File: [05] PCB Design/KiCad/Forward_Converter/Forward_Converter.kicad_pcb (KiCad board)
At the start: 2 copper layers, 75 parts, among them J1 Conn_01x02_Pin, J2 Conn_01x02_Pin, J3 Conn_01x02_Pin, J4 Conn_01x02_Pin, J5 Conn_01x02_Pin, Q1 CSD19534Q5A, Q2 CSD19534Q5A, Q3 BSC320N20NS3G, Q4 BCX56, Q5 BC857, Q6 BCX56, T1 P0926NL, T2 EE30157-Custom, U1 LT1952EGN-1-PBF, U2 LTC3900ES8-PBF, U3 MC7812CDTRKG, U4 LT4430ES6-TRPBF, U5 TCMT1106

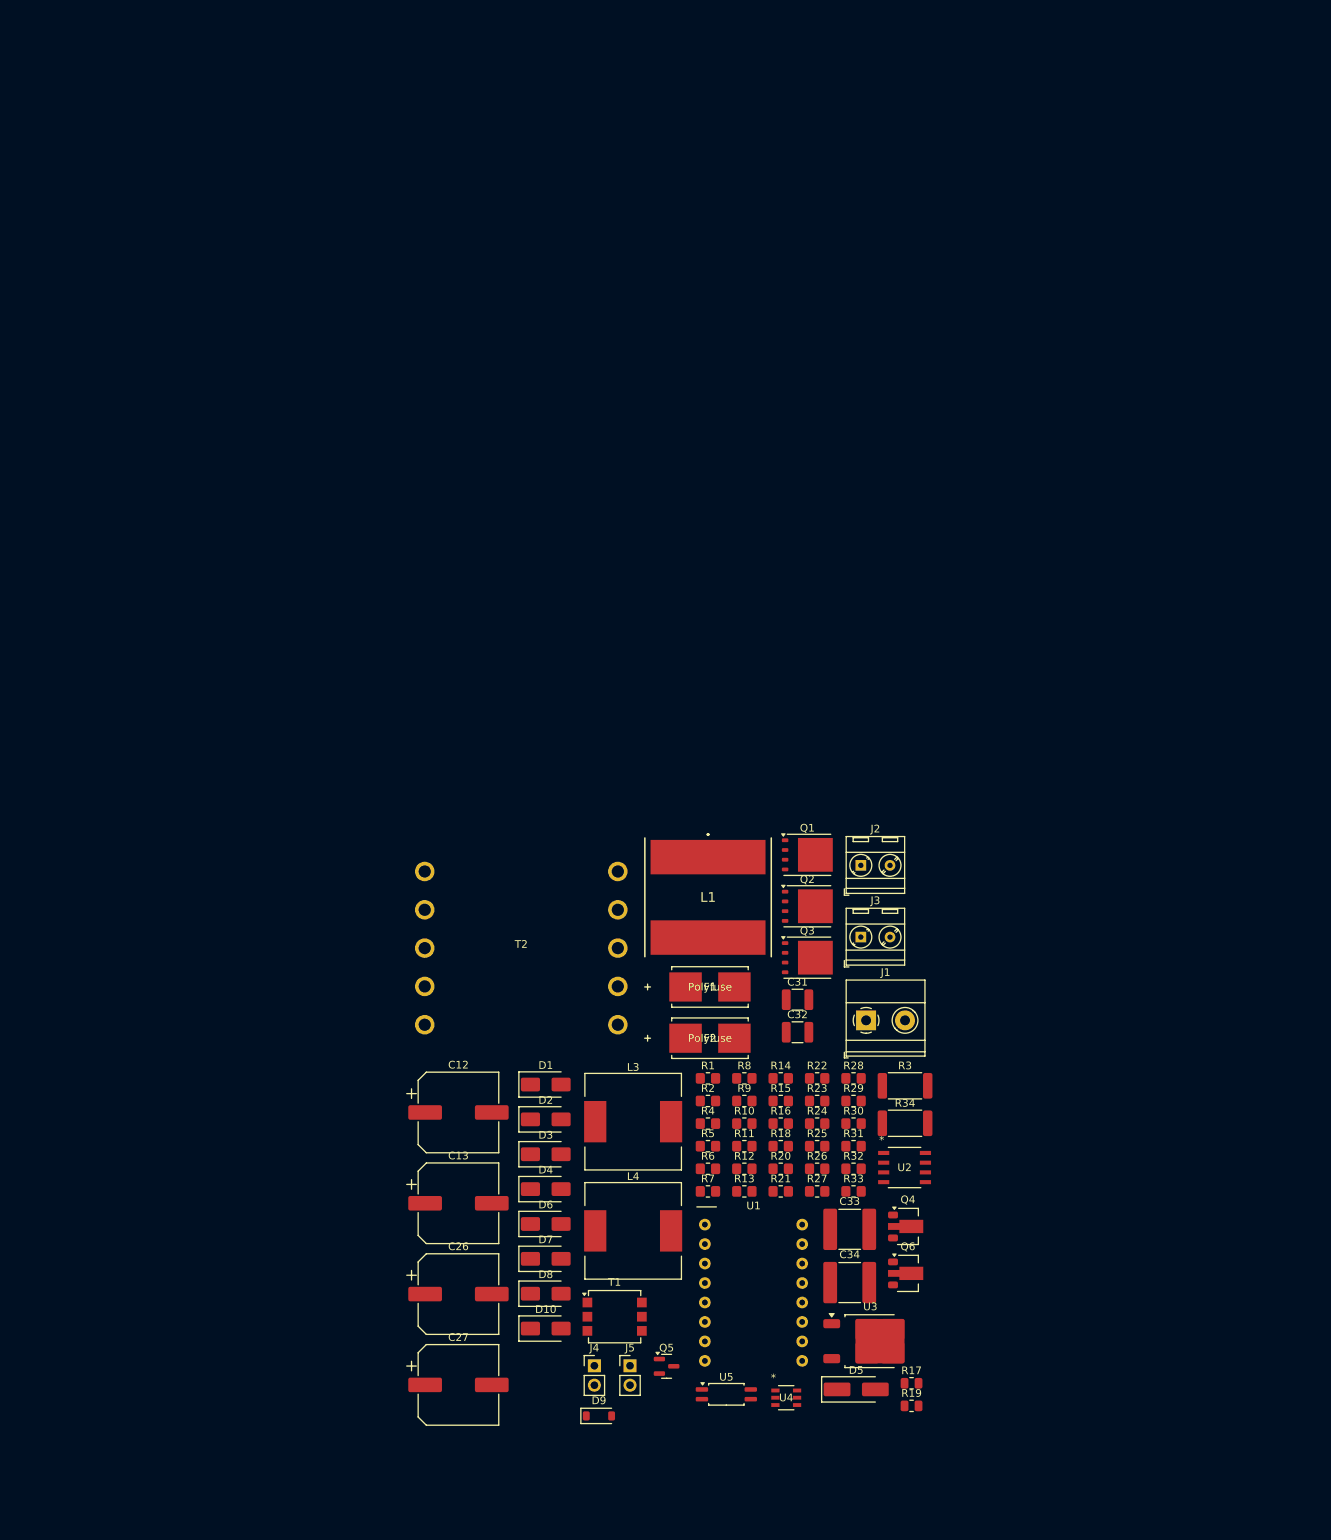
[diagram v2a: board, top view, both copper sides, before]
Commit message: Layout placement
Placement is almost complete connections to be completed.
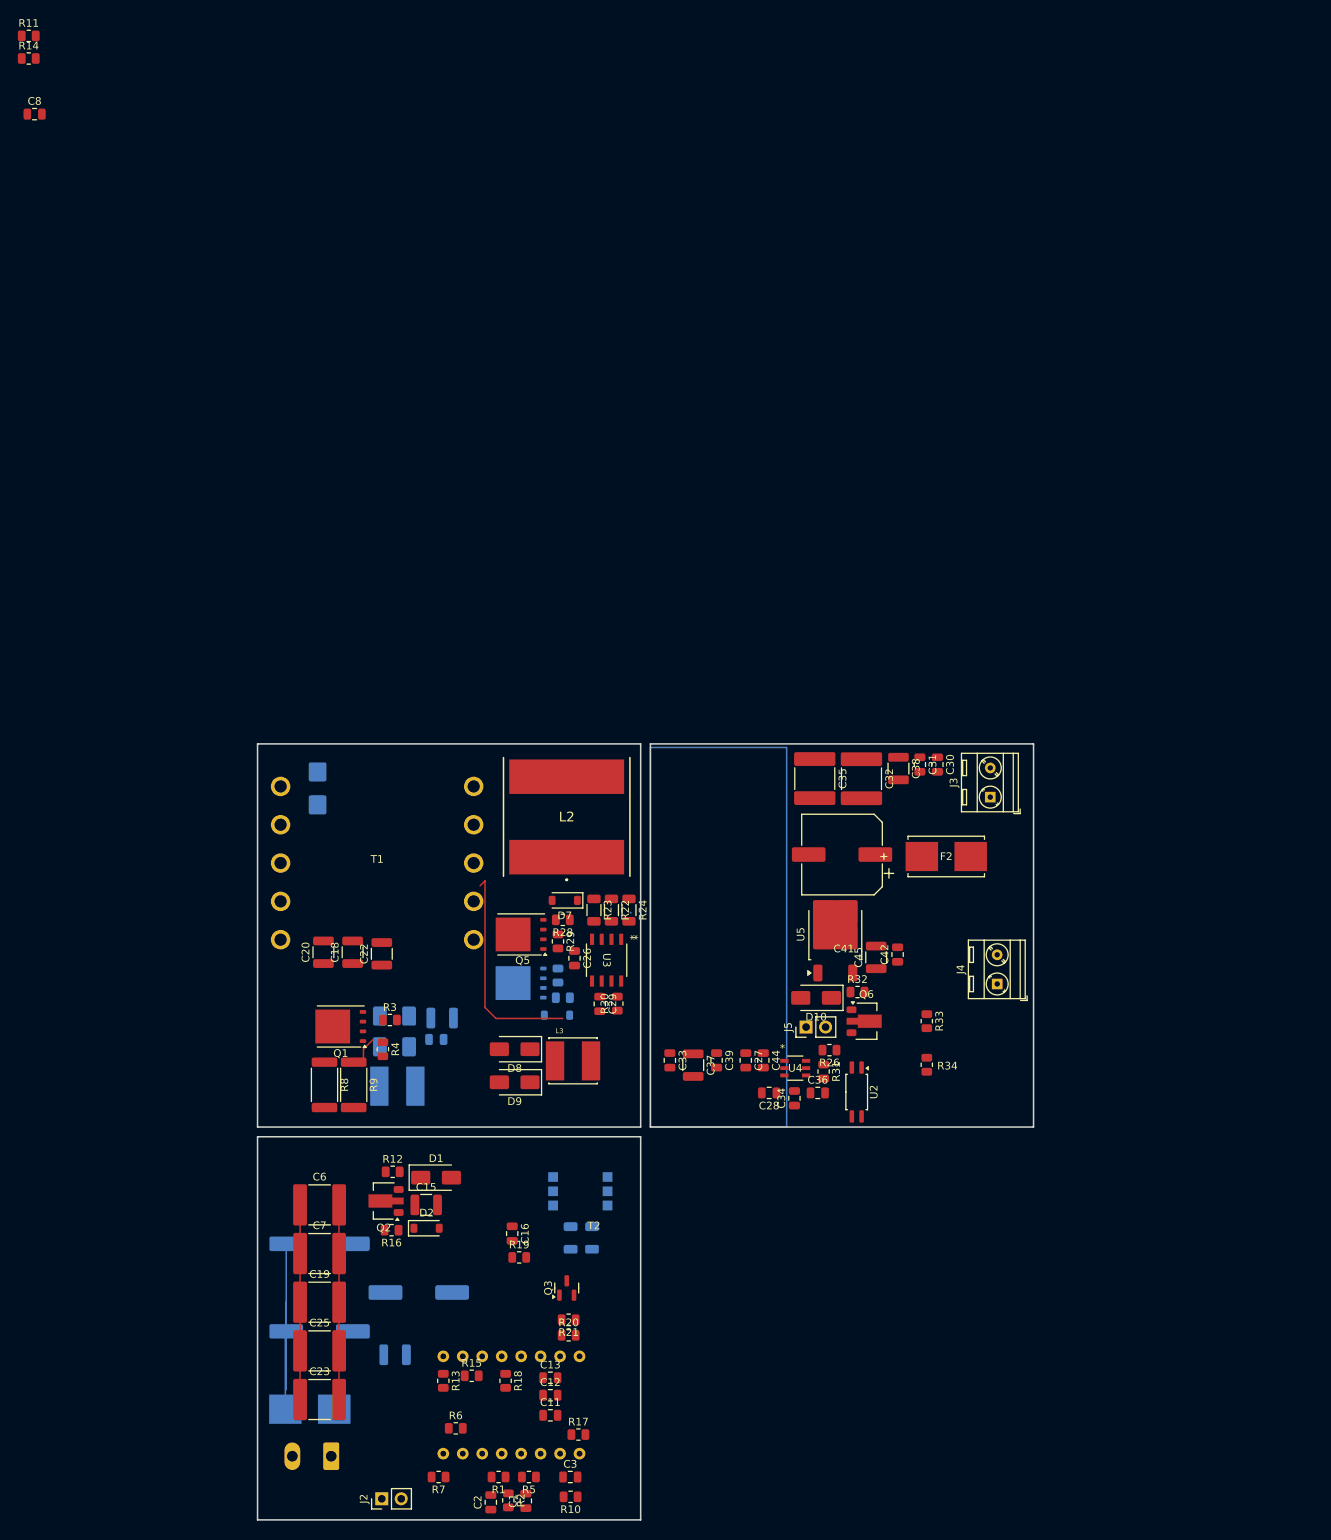
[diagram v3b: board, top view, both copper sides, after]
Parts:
- removed L4: 22uH, Inductor_SMD:L_12x12mm_H6mm
- added C1: 2.2nF, Capacitor_SMD:C_0805_2012Metric, F.Cu at (72.6, 125.0)
- added C10: 10u, Capacitor_SMD:C_1210_3225Metric, B.Cu at (55.6, 105.9)
- added C11: 2.2uF, Capacitor_SMD:C_0805_2012Metric, F.Cu at (75.8, 113.8)
- added C14: 10u, Capacitor_SMD:C_1210_3225Metric, B.Cu at (61.7, 62.0)
- added C15: 1uF, Capacitor_SMD:C_1210_3225Metric, F.Cu at (59.6, 86.4)
- added C16: 2.2nF, Capacitor_SMD:C_0805_2012Metric, F.Cu at (70.9, 90.1)
- added C17: 100n, Capacitor_SMD:C_0805_2012Metric, B.Cu at (61.0, 64.8)
- added C18: 1uF, Capacitor_SMD:C_1210_3225Metric, F.Cu at (50.0, 53.4)
- added C19: 2.2u, Capacitor_SMD:C_2220_5750Metric, F.Cu at (45.7, 99.1)
- added C2: 100nF, Capacitor_SMD:C_0805_2012Metric, F.Cu at (68.1, 125.2)
- added C20: 1uF, Capacitor_SMD:C_1210_3225Metric, F.Cu at (46.2, 53.4)
- added C21: 100pF, Capacitor_SMD:C_1206_3216Metric, B.Cu at (81.3, 90.7)
- added C22: 1uF, Capacitor_SMD:C_1210_3225Metric, F.Cu at (53.8, 53.6)
- added C23: 2.2u, Capacitor_SMD:C_2220_5750Metric, F.Cu at (45.7, 111.8)
- added C24: 220pF, Capacitor_SMD:C_1206_3216Metric, B.Cu at (78.5, 90.7)
- added C25: 2.2u, Capacitor_SMD:C_2220_5750Metric, F.Cu at (45.7, 105.4)
- added C28: 100p, Capacitor_SMD:C_0805_2012Metric, F.Cu at (104.4, 71.8)
- added C29: 470p, Capacitor_SMD:C_0805_2012Metric, F.Cu at (82.3, 60.1)
- added C3: OC, Capacitor_SMD:C_0805_2012Metric, F.Cu at (78.4, 121.9)
- added C30: 100n, Capacitor_SMD:C_0805_2012Metric, F.Cu at (126.4, 28.9)
- added C35: 2.2u, Capacitor_SMD:C_2220_5750Metric, F.Cu at (110.4, 30.7)
- added C36: 10n, Capacitor_SMD:C_0805_2012Metric, F.Cu at (110.7, 71.8)
- added C37: 10u, Capacitor_SMD:C_1210_3225Metric, F.Cu at (94.5, 68.1)
- added C38: 22u, Capacitor_SMD:C_1210_3225Metric, F.Cu at (121.3, 29.4)
- added C39: 100n, Capacitor_SMD:C_0805_2012Metric, F.Cu at (97.5, 67.5)
- added C4: 47u, Capacitor_SMD:CP_Elec_10x12.6, B.Cu at (45.7, 91.4)
- added C41: 180u, Capacitor_SMD:CP_Elec_10x12.6, F.Cu at (113.9, 40.6)
- added C42: 100n, Capacitor_SMD:C_0805_2012Metric, F.Cu at (121.2, 53.7)
- added C44: 100n, Capacitor_SMD:C_0805_2012Metric, F.Cu at (103.6, 67.5)
- added C45: 10u, Capacitor_SMD:C_1210_3225Metric, F.Cu at (118.4, 54.1)
- added C5: 47u, Capacitor_SMD:CP_Elec_10x12.6, B.Cu at (45.7, 102.9)
- added C6: 2.2uF, Capacitor_SMD:C_2220_5750Metric, F.Cu at (45.7, 86.4)
- added C7: 2.2uF, Capacitor_SMD:C_2220_5750Metric, F.Cu at (45.7, 92.7)
- added C8: 2.2nF, Capacitor_SMD:C_0805_2012Metric, F.Cu at (8.54, -56.0)
- added C9: 47u, Capacitor_SMD:CP_Elec_10x12.6, B.Cu at (58.7, 97.8)
- added L2: 22uH, Forward_Footprint:SRP1513CA8R2M_V2, F.Cu at (78.0, 35.7)
- C12, C13: value 180u -> 100nF; footprint Capacitor_SMD:CP_Elec_10x12.6 -> Capacitor_SMD:C_0805_2012Metric
- C26: value 47u -> 100n; footprint Capacitor_SMD:CP_Elec_10x12.6 -> Capacitor_SMD:C_0805_2012Metric
- C27: value 47u -> 1uF; footprint Capacitor_SMD:CP_Elec_10x12.6 -> Capacitor_SMD:C_0805_2012Metric
- C31: value 1uF -> 100n; footprint Capacitor_SMD:C_1210_3225Metric -> Capacitor_SMD:C_0805_2012Metric
- C32: value 1uF -> 2.2u; footprint Capacitor_SMD:C_1210_3225Metric -> Capacitor_SMD:C_2220_5750Metric
- C33: value 2.2u -> 100n; footprint Capacitor_SMD:C_2220_5750Metric -> Capacitor_SMD:C_0805_2012Metric
- C34: value 2.2u -> 220p; footprint Capacitor_SMD:C_2220_5750Metric -> Capacitor_SMD:C_0805_2012Metric
- D1: value MS110 -> 1SMA5931
- D10: value 1SMA5931 -> SMAJ4737A
- D2: value MS110 -> BZT52C12-TP; footprint Diode_SMD:D_SMA -> Diode_SMD:D_SOD-123
- D3, F1, U1: moved to B.Cu
- D4: value MS110 -> BR320; footprint Diode_SMD:D_SMA -> Diode_SMD:D_SMB; moved to B.Cu
- D5: value SMAJ4737A -> MS110; footprint Diode_SMD:D_SMA_Handsoldering -> Diode_SMD:D_SMA; moved to B.Cu
- D6: footprint Diode_SMD:D_SMA -> Diode_SMD:D_SOD-123; moved to B.Cu
- D7: footprint Diode_SMD:D_SMA -> Diode_SMD:D_SOD-123
- D8: value BR320 -> MS110
- D9: value BZT52C12-TP -> MS110; footprint Diode_SMD:D_SOD-123 -> Diode_SMD:D_SMA
- J1: value Conn_01x02_Pin -> INPUT; footprint TerminalBlock_Phoenix:TerminalBlock_Phoenix_MKDS-1,5-2-5.08_1x02_P5.08mm_Horizontal -> Connector_Phoenix_MSTB:PhoenixContact_MSTBA_2,5_2-G-5,08_1x02_P5.08mm_Horizontal; moved to B.Cu
- J2: value Conn_01x02_Pin -> BIAS; footprint TerminalBlock_MetzConnect:TerminalBlock_MetzConnect_Type086_RT03402HBLC_1x02_P3.81mm_Horizontal -> Connector_PinHeader_2.54mm:PinHeader_1x02_P2.54mm_Vertical
- J3: value Conn_01x02_Pin -> OUTPUT
- J4: value Conn_01x02_Pin -> AUX; footprint Connector_PinHeader_2.54mm:PinHeader_1x02_P2.54mm_Vertical -> TerminalBlock_MetzConnect:TerminalBlock_MetzConnect_Type086_RT03402HBLC_1x02_P3.81mm_Horizontal
- J5: value Conn_01x02_Pin -> 8V
- L1: value 22uH -> 10uH; footprint Forward_Footprint:SRP1513CA8R2M_V2 -> Forward_Footprint:IND_VLS6045EX-100M-H; moved to B.Cu
- L3: value 22uH -> 10uH; footprint Inductor_SMD:L_12x12mm_H6mm -> Forward_Footprint:IND_VLS6045EX-100M-H
- Q1: value CSD19534Q5A -> BSC320N20NS3G
- Q2: value CSD19534Q5A -> BCX56; footprint Package_TO_SOT_SMD:TDSON-8-1 -> Package_TO_SOT_SMD:SOT-89-3
- Q3: value BSC320N20NS3G -> BC857; footprint Package_TO_SOT_SMD:TDSON-8-1 -> Package_TO_SOT_SMD:SOT-23
- Q4: value BCX56 -> CSD19534Q5A; footprint Package_TO_SOT_SMD:SOT-89-3 -> Package_TO_SOT_SMD:TDSON-8-1; moved to B.Cu
- Q5: value BC857 -> CSD19534Q5A; footprint Package_TO_SOT_SMD:SOT-23 -> Package_TO_SOT_SMD:TDSON-8-1
- R1: value 12R -> 12k; footprint Resistor_SMD:R_0805_2012Metric_Pad1.20x1.40mm_HandSolder -> Resistor_SMD:R_0805_2012Metric
- R10: value 180k -> 10k; footprint Resistor_SMD:R_0805_2012Metric_Pad1.20x1.40mm_HandSolder -> Resistor_SMD:R_0805_2012Metric
- R11: value 100k -> 0; footprint Resistor_SMD:R_0805_2012Metric_Pad1.20x1.40mm_HandSolder -> Resistor_SMD:R_0805_2012Metric
- R12: value 160k -> 4.7k; footprint Resistor_SMD:R_0805_2012Metric_Pad1.20x1.40mm_HandSolder -> Resistor_SMD:R_0805_2012Metric
- R13: value 10k -> 100k; footprint Resistor_SMD:R_0805_2012Metric_Pad1.20x1.40mm_HandSolder -> Resistor_SMD:R_0805_2012Metric
- R14: value 10k -> 0; footprint Resistor_SMD:R_0805_2012Metric_Pad1.20x1.40mm_HandSolder -> Resistor_SMD:R_0805_2012Metric
- R15: value 10k -> 0R; footprint Resistor_SMD:R_0805_2012Metric_Pad1.20x1.40mm_HandSolder -> Resistor_SMD:R_0805_2012Metric
- R16: value 25 -> 4.7k; footprint Resistor_SMD:R_0805_2012Metric_Pad1.20x1.40mm_HandSolder -> Resistor_SMD:R_0805_2012Metric
- R17: value 22k -> 10k
- R18: value 25 -> 160k; footprint Resistor_SMD:R_0805_2012Metric_Pad1.20x1.40mm_HandSolder -> Resistor_SMD:R_0805_2012Metric
- R19: value 22k -> 47R
- R2: value 10k -> 18k; footprint Resistor_SMD:R_0805_2012Metric_Pad1.20x1.40mm_HandSolder -> Resistor_SMD:R_0805_2012Metric
- R20: value 47R -> 220R; footprint Resistor_SMD:R_0805_2012Metric_Pad1.20x1.40mm_HandSolder -> Resistor_SMD:R_0805_2012Metric
- R21: value 200k -> 1.2k; footprint Resistor_SMD:R_0805_2012Metric_Pad1.20x1.40mm_HandSolder -> Resistor_SMD:R_0805_2012Metric
- R22: value 27k -> 360; footprint Resistor_SMD:R_0805_2012Metric_Pad1.20x1.40mm_HandSolder -> Resistor_SMD:R_1206_3216Metric
- R23: value 8.2k -> 182; footprint Resistor_SMD:R_0805_2012Metric_Pad1.20x1.40mm_HandSolder -> Resistor_SMD:R_1206_3216Metric
- R24: value 4.7k -> 365; footprint Resistor_SMD:R_0805_2012Metric_Pad1.20x1.40mm_HandSolder -> Resistor_SMD:R_1206_3216Metric
- R25: value 1.2k -> 25; footprint Resistor_SMD:R_0805_2012Metric_Pad1.20x1.40mm_HandSolder -> Resistor_SMD:R_0805_2012Metric; moved to B.Cu
- R26: value 220R -> 4.7k; footprint Resistor_SMD:R_0805_2012Metric_Pad1.20x1.40mm_HandSolder -> Resistor_SMD:R_0805_2012Metric
- R27: value 10k -> 22k; footprint Resistor_SMD:R_0805_2012Metric_Pad1.20x1.40mm_HandSolder -> Resistor_SMD:R_0805_2012Metric; moved to B.Cu
- R28: value 1k -> 25; footprint Resistor_SMD:R_0805_2012Metric_Pad1.20x1.40mm_HandSolder -> Resistor_SMD:R_0805_2012Metric
- R29: value 4.7k -> 22k; footprint Resistor_SMD:R_0805_2012Metric_Pad1.20x1.40mm_HandSolder -> Resistor_SMD:R_0805_2012Metric
- R3: value 15m -> 12R; footprint Resistor_SMD:R_2512_6332Metric -> Resistor_SMD:R_0805_2012Metric
- R30: value 4.7k -> 100k; footprint Resistor_SMD:R_0805_2012Metric_Pad1.20x1.40mm_HandSolder -> Resistor_SMD:R_0805_2012Metric
- R31: value 0R -> 8.2k; footprint Resistor_SMD:R_0805_2012Metric_Pad1.20x1.40mm_HandSolder -> Resistor_SMD:R_0805_2012Metric
- R32: value 0 -> 1k; footprint Resistor_SMD:R_0805_2012Metric_Pad1.20x1.40mm_HandSolder -> Resistor_SMD:R_0805_2012Metric
- R33: value 0 -> 200k; footprint Resistor_SMD:R_0805_2012Metric_Pad1.20x1.40mm_HandSolder -> Resistor_SMD:R_0805_2012Metric
- R34: value 15m -> 27k; footprint Resistor_SMD:R_2512_6332Metric -> Resistor_SMD:R_0805_2012Metric
- R4: value 12k -> 10k; footprint Resistor_SMD:R_0805_2012Metric_Pad1.20x1.40mm_HandSolder -> Resistor_SMD:R_0805_2012Metric
- R5: value 10k -> 180k; footprint Resistor_SMD:R_0805_2012Metric_Pad1.20x1.40mm_HandSolder -> Resistor_SMD:R_0805_2012Metric
- R6: footprint Resistor_SMD:R_0805_2012Metric_Pad1.20x1.40mm_HandSolder -> Resistor_SMD:R_0805_2012Metric
- R7: value 18k -> 10k; footprint Resistor_SMD:R_0805_2012Metric_Pad1.20x1.40mm_HandSolder -> Resistor_SMD:R_0805_2012Metric
- R8: value 47R -> 15m; footprint Resistor_SMD:R_0805_2012Metric_Pad1.20x1.40mm_HandSolder -> Resistor_SMD:R_2512_6332Metric
- R9: value 10k -> 15m; footprint Resistor_SMD:R_0805_2012Metric_Pad1.20x1.40mm_HandSolder -> Resistor_SMD:R_2512_6332Metric
- T1: value P0926NL -> EE30157-Custom; footprint Transformer_SMD:Pulse_P0926NL -> Forward_Footprint:EE30157-Custom
- T2: value EE30157-Custom -> P0926NL; footprint Forward_Footprint:EE30157-Custom -> Transformer_SMD:Pulse_P0926NL; moved to B.Cu
- U2: value LTC3900ES8-PBF -> TCMT1106; footprint Forward_Footprint:SO-8_S_LIT -> Package_SO:SOP-4_4.4x2.6mm_P1.27mm
- U3: value MC7812CDTRKG -> LTC3900ES8-PBF; footprint Package_TO_SOT_SMD:TO-252-2 -> Forward_Footprint:SO-8_S_LIT
- U5: value TCMT1106 -> MC7812CDTRKG; footprint Package_SO:SOP-4_4.4x2.6mm_P1.27mm -> Package_TO_SOT_SMD:TO-252-2
- moved R11 172.4 mm to (7.77, -66.2)
- moved R14 165.4 mm to (7.77, -63.2)
- moved J2 103.6 mm to (53.8, 124.7), turned to 90 degrees
- moved J1 90.0 mm to (47.2, 119.2), turned to 180 degrees
- moved D5 77.8 mm to (53.6, 63.7), turned to 90 degrees
- moved F1 75.9 mm to (44.5, 113.0), turned to 180 degrees
- moved J4 72.4 mm to (134.2, 57.5), turned to 90 degrees
- moved R3 67.8 mm to (54.9, 62.2)
- moved Q2 67.3 mm to (54.1, 85.9), turned to 180 degrees
- moved T1 66.8 mm to (53.2, 41.8)
- moved Q1 64.9 mm to (48.5, 63.1), turned to 180 degrees
- moved U5 61.7 mm to (113.0, 51.1), turned to 90 degrees
- moved U3 60.5 mm to (83.2, 54.4), turned to -90 degrees
- moved D4 60.2 mm to (45.5, 32.0), turned to 90 degrees
- moved Q4 59.6 mm to (72.0, 57.4), turned to 180 degrees
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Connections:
- C12 pad 1: /5V -> GND
- C12 pad 2: GNDPWR -> /Vbias
- C13 pad 1: /5V -> GND
- C13 pad 2: GNDPWR -> /Vbias
- C26 pad 1: Vin -> /8V
- C26 pad 2: PGND -> GNDSEC
- C27 pad 1: Vin -> /8V
- C27 pad 2: PGND -> GNDSEC
- C31 pad 1: Vin -> /5V
- C31 pad 2: PGND -> GNDPWR
- C32 pad 1: Vin -> /5V
- C32 pad 2: PGND -> GNDPWR
- C33 pad 1: Vin -> Net-(U5-VI)
- C33 pad 2: PGND -> GNDSEC
- C34 pad 1: Vin -> Net-(U4-FB)
- C34 pad 2: PGND -> Net-(U4-COMP)
- D1 pad 1: Net-(D1-K) -> /Vbias
- D10 pad 1: /Vbias -> Net-(D10-A1)
- D10 pad 2: GND -> GNDSEC
- D2 pad 2: GNDSEC -> GND
- D3 pad 1: Net-(D2-K) -> Net-(D3-K)
- D3 pad 2: /Vaux -> GND
- D4 pad 1: Net-(D1-K) -> /RST
- D4 pad 2: /AUX -> PGND
- D5 pad 1: Net-(D5-A1) -> Net-(D3-K)
- D5 pad 2: GNDSEC -> /AUX
- D8 pad 1: /RST -> Net-(D8-K)
- D8 pad 2: PGND -> /Vaux
- D9 pad 1: Net-(D9-K) -> Net-(D8-K)
- D9 pad 2: GND -> GNDSEC
- F2 pad 2: Net-(J2-Pin_1) -> Net-(J3-Pin_1)
- J2 pad 1: Net-(J2-Pin_1) -> /Vbias
- J2 pad 2: GNDPWR -> GND
- J3 pad 1: /12V -> Net-(J3-Pin_1)
- J3 pad 2: GNDSEC -> GNDPWR
- J4 pad 1: GNDSEC -> /12V
- J4 pad 2: /8V -> GNDSEC
- J5 pad 1: /Vbias -> GNDSEC
- J5 pad 2: GND -> /8V
- L1 pad 1: /VSEC+ -> Net-(Q2-C)
- L1 pad 2: /5V -> Net-(D3-K)
- L3 pad 1: Net-(Q6-C) -> Net-(D8-K)
- L3 pad 2: Net-(D1-K) -> Net-(U5-VI)
- Q1 pad 1: GNDPWR -> /Isense
- Q1 pad 2: GNDPWR -> /Isense
- Q1 pad 3: GNDPWR -> /Isense
- Q1 pad 4: Net-(D6-A) -> Net-(Q1-G)
- Q1 pad 5: /VSEC- -> /Vsw
- Q2 pad 1: GNDPWR -> Net-(D2-K)
- Q2 pad 2: GNDPWR -> Net-(Q2-C)
- Q2 pad 3: GNDPWR -> /Vbias
- Q3 pad 1: /Isense -> /VREF
- Q3 pad 2: /Isense -> Net-(Q3-E)
- Q3 pad 3: /Isense -> GND
- Q4 pad 1: Net-(D5-A1) -> GNDPWR
- Q4 pad 2: /12V -> GNDPWR
- Q4 pad 3: /8V -> GNDPWR
- Q5 pad 1: /VREF -> GNDPWR
- Q5 pad 2: Net-(Q5-E) -> GNDPWR
- Q5 pad 3: GND -> GNDPWR
- Q6 pad 1: Net-(D9-K) -> Net-(D10-A1)
- Q6 pad 2: Net-(Q6-C) -> /12V
- Q6 pad 3: /Vbias -> /8V
- R1 pad 1: Net-(Q3-G) -> Net-(U1-SS_MAXDC)
- R1 pad 2: /GATEOUT -> /VREF
- R10 pad 1: Net-(U1-ROSC) -> Net-(U1-COMP)
- R10 pad 2: GND -> /FB
- R11 pad 1: Net-(U1-BLANK) -> PGND
- R12 pad 1: Net-(U1-DELAY) -> Vin
- R12 pad 2: GND -> /Vbias
- R13 pad 1: /VSEC+ -> Net-(U1-BLANK)
- R13 pad 2: Net-(U2-CS+) -> GND
- R14 pad 2: Net-(U2-CS+) -> GNDPWR
- R15 pad 1: GNDSEC -> Net-(U1-ISENSE)
- R15 pad 2: Net-(U2-CS-) -> Net-(U1-OC)
- R16 pad 1: /FG -> Net-(D2-K)
- R16 pad 2: Net-(D6-A) -> Net-(Q2-C)
- R17 pad 1: Net-(D6-A) -> /FB
- R17 pad 2: GNDPWR -> Net-(Q3-E)
- R18 pad 1: /CG -> Net-(U1-DELAY)
- R18 pad 2: Net-(D7-A) -> GND
- R19 pad 1: Net-(D7-A) -> Net-(U1-OC)
- R19 pad 2: GNDPWR -> /Isense
- R2 pad 1: Net-(Q3-G) -> Net-(U1-SS_MAXDC)
- R2 pad 2: PGND -> GND
- R20 pad 1: Net-(U2-TIMER) -> /Vbias
- R20 pad 2: /8V -> Net-(R20-Pad2)
- R21 pad 1: /5V -> Net-(Q3-E)
- R21 pad 2: Net-(U4-FB) -> GND
- R22 pad 1: Net-(U4-FB) -> GNDSEC
- R22 pad 2: GNDSEC -> Net-(U3-CS+)
- R23 pad 1: Net-(U4-COMP) -> GNDSEC
- R23 pad 2: Net-(C16-Pad2) -> Net-(U3-CS-)
- R24 pad 1: Net-(R24-Pad1) -> /VSEC+
- R24 pad 2: Net-(U4-OPTO) -> Net-(U3-CS+)
- R25 pad 1: Net-(Q5-E) -> /FG
- R25 pad 2: GND -> Net-(D6-A)
- R26 pad 1: /Vbias -> Net-(R26-Pad1)
- R26 pad 2: Net-(R26-Pad2) -> Net-(U4-OPTO)
- R27 pad 1: /FB -> Net-(D6-A)
- R27 pad 2: Net-(Q5-E) -> GNDPWR
- R28 pad 1: Net-(D5-A1) -> /CG
- R28 pad 2: /12V -> Net-(D7-A)
- R29 pad 1: Net-(D9-K) -> Net-(D7-A)
- R29 pad 2: Net-(Q6-C) -> GNDPWR
- R3 pad 1: /Isense -> Net-(Q1-G)
- R3 pad 2: PGND -> /GATEOUT
- R30 pad 1: Vin -> Net-(U3-TIMER)
- R30 pad 2: /Vbias -> /8V
- R31 pad 1: Net-(U1-ISENSE) -> Net-(U4-COMP)
- R31 pad 2: Net-(U1-OC) -> Net-(C36-Pad2)
- R32 pad 1: PGND -> Net-(D10-A1)
- R32 pad 2: GND -> /12V
- R33 pad 1: GNDSEC -> /5V
- R33 pad 2: GNDPWR -> Net-(U4-FB)
- R34 pad 1: /Isense -> Net-(U4-FB)
- R34 pad 2: PGND -> GNDSEC
- R4 pad 1: Net-(U1-SS_MAXDC) -> Net-(Q1-G)
- R4 pad 2: /VREF -> PGND
- R5 pad 1: Net-(U1-SD_VSEC) -> Net-(U1-ROSC)
- R7 pad 1: Net-(U1-SS_MAXDC) -> Net-(U1-SD_VSEC)
- R8 pad 1: Net-(U1-OC) -> /Isense
- R8 pad 2: /Isense -> PGND
- R9 pad 1: Net-(U1-COMP) -> /Isense
- R9 pad 2: /FB -> PGND
- T1 pad 1: Net-(C8-Pad1) -> GND
- T1 pad 2: unconnected-(T1-Pad2) -> /AUX
- T1 pad 3: GNDSEC -> /RST
- T1 pad 4: Net-(U2-SYNC) -> /Vsw
- T1 pad 5: unconnected-(T1-Pad5) -> Vin
- T1 pad 6: GND -> (no net)
- T2 pad 1: Vin -> Net-(C24-Pad1)
- T2 pad 2: /Vsw -> unconnected-(T2-Pad2)
- T2 pad 3: /RST -> GNDSEC
- T2 pad 4: /AUX -> Net-(U3-SYNC)
- T2 pad 5: GND -> unconnected-(T2-Pad5)
- T2 pad 6: (no net) -> GND
- U2 pad 1: Net-(U2-CS+) -> Net-(R26-Pad1)
- U2 pad 2: Net-(U2-CS-) -> GNDSEC
- U2 pad 3: /CG -> Net-(Q3-E)
- U2 pad 4: /8V -> Net-(R20-Pad2)
- U3 pad 1: /12V -> Net-(U3-CS+)
- U3 pad 2: GNDSEC -> Net-(U3-CS-)
- U3 pad 3: Net-(U3-VO) -> /CG
- U5 pad 1: Net-(R24-Pad1) -> Net-(U5-VI)
- U5 pad 3: Net-(Q5-E) -> /12V
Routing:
- net Vin: track 0.00 -> 58.5 mm
- net /5V: track 0.00 -> 28.2 mm
- net PGND: track 0.00 -> 25.4 mm
- net /Isense: track 0.00 -> 3.91 mm
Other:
- board outline added: 101.3 x 101.3 mm
- board text added: "PRI"
- board text added: "SEC"
- board text added: "XFORMER"

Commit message: [05] schematic with zero percent battery
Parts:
- C17: moved to F.Cu
- C18, C20, C22, C30, C31, C38: moved to B.Cu
- moved C30 57.4 mm to (69.7, 38.2)
- moved C31 52.9 mm to (72.0, 38.2)
- moved C38 47.4 mm to (74.8, 38.7)
- moved C22 30.2 mm to (44.7, 82.4), turned to 0 degrees
- moved D4 21.1 mm to (48.1, 53.0), turned to -90 degrees
- moved C17 18.3 mm to (68.9, 81.3)
- moved C14 11.2 mm to (58.8, 72.8), turned to 0 degrees
- moved C20 10.5 mm to (46.9, 63.9), turned to 0 degrees
- moved C18 7.36 mm to (46.9, 60.1), turned to 0 degrees
- moved L3 3.43 mm to (79.7, 70.9)
- moved D8 3.43 mm to (72.1, 69.3)
- moved D9 3.43 mm to (72.1, 73.7)
- moved D3 3.06 mm to (57.7, 60.7)
- moved D5 3.06 mm to (53.8, 60.7)
- moved L1 3.06 mm to (56.1, 67.8)
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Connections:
- T1 pad 10: GNDSEC -> /VSEC-
- T1 pad 6: (no net) -> GNDSEC
- T1 pad 7: /VSEC+ -> /Vaux
- T1 pad 8: /VSEC- -> (no net)
- T1 pad 9: /Vaux -> /VSEC+
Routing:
- net Vin: track 58.5 -> 0.15 mm
- net /5V: track 28.2 -> 0.00 mm
- net PGND: track 25.4 -> 0.00 mm, vias 0 -> 2
- net /Isense: track 3.91 -> 0.00 mm
- net Net-(Q2-C): vias 0 -> 1
- net GNDPWR: vias 0 -> 2
- net (no net): vias 0 -> 3
- added copper zone on B.Cu, net /5V
- added copper zone on F.Cu, net /5V
- added copper zone on F.Cu, net /8V
- added copper zone on B.Cu, net /AUX
- added copper zone on F.Cu, net /CG
- added copper zone on F.Cu, net /Isense
- added copper zone on B.Cu, net /RST
- added copper zone on F.Cu, net /VSEC+
- added copper zone on B.Cu, net /VSEC-
- added copper zone on B.Cu, net /Vbias
- added copper zone on F.Cu, net /Vbias
- added copper zone on F.Cu, net /Vsw
- added copper zone on B.Cu, net GND
- added copper zone on B.Cu, net GNDPWR
- added copper zone on F.Cu, net GNDPWR
- added copper zone on F.Cu, net Net-(D2-K)
- added copper zone on F.Cu, net Net-(D7-A)
- added copper zone on B.Cu, net Net-(J1-Pin_1)
- added copper zone on B.Cu, net Net-(Q2-C)
- added copper zone on F.Cu, net Net-(Q2-C)
- added copper zone on F.Cu, net Net-(U3-CS-)
- added copper zone on B.Cu, net PGND
- added copper zone on F.Cu, net PGND
- added copper zone on B.Cu, net Vin
- added copper zone on F.Cu, net Vin
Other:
- outline, holes or cut-outs redrawn

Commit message: Layout is updated
Close to the final result
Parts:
- C19, C25, C6, C7, D8, D9, R20, R6: moved to B.Cu
- C21, C24, C4, C5, C9, D6, R25, T2: moved to F.Cu
- moved D9 40.2 mm to (60.8, 35.1), turned to 45 degrees
- moved D8 31.0 mm to (61.5, 40.3), turned to 45 degrees
- moved D3 29.3 mm to (47.1, 33.3), turned to 135 degrees
- moved D5 23.3 mm to (46.8, 38.5), turned to 135 degrees
- moved C23 22.1 mm to (45.3, 89.7)
- moved C11 21.2 mm to (55.1, 109.6), turned to 180 degrees
- moved C12 20.8 mm to (55.1, 112.2), turned to 180 degrees
- moved J2 19.5 mm to (54.3, 105.4)
- moved Q3 19.0 mm to (83.6, 115.4), turned to 0 degrees
- moved R21 18.2 mm to (83.7, 118.7), turned to 0 degrees
- moved C17 17.3 mm to (55.1, 91.7), turned to 0 degrees
- moved R34 13.9 mm to (111.5, 71.5), turned to 90 degrees
- moved C16 13.4 mm to (67.1, 103.0)
- moved C41 13.0 mm to (124.9, 33.7), turned to -90 degrees
- moved R6 10.9 mm to (54.4, 109.6)
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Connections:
- R4 pad 2: PGND -> /Isense
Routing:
- net GNDSEC: track 0.00 -> 96.2 mm, vias 0 -> 1
- net GND: track 0.00 -> 88.8 mm, vias 0 -> 3
- net /GATEOUT: track 0.00 -> 50.3 mm
- net /Isense: track 0.00 -> 47.0 mm
- net Net-(D8-K): track 0.00 -> 42.2 mm, vias 0 -> 1
- net /8V: track 0.00 -> 38.0 mm, vias 0 -> 2
- net Net-(D3-K): track 0.00 -> 34.5 mm
- net Net-(U3-SYNC): track 0.00 -> 32.7 mm, vias 0 -> 2
- net Net-(U5-VI): track 0.00 -> 30.2 mm, vias 0 -> 2
- net /Vbias: track 0.00 -> 28.4 mm, vias 0 -> 1
- net PGND: track 0.00 -> 25.7 mm
- net /VREF: track 0.00 -> 23.0 mm
- net Net-(U1-SD_VSEC): track 0.00 -> 19.2 mm
- net Vin: track 0.15 -> 15.0 mm
- net Net-(Q3-E): track 0.00 -> 12.2 mm
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- added copper zone on F.Cu, net /12V
- added copper zone on F.Cu, net /AUX
- added copper zone on F.Cu, net /RST
- added copper zone on B.Cu, net /Vaux
- added copper zone on F.Cu, net GND
- added copper zone on B.Cu, net GNDSEC
- added copper zone on F.Cu, net GNDSEC
- added copper zone on F.Cu, net Net-(D10-A1)
- added copper zone on B.Cu, net Net-(D6-A)
- added copper zone on F.Cu, net Net-(D6-A)
- added copper zone on F.Cu, net Net-(D8-K)
- added copper zone on F.Cu, net Net-(J3-Pin_1)
- added copper zone on F.Cu, net Net-(Q1-G)
- added copper zone on F.Cu, net Net-(U3-CS+)
- added copper zone on F.Cu, net Net-(U3-SYNC)
- added copper zone on B.Cu, net Net-(U5-VI)
- added copper zone on F.Cu, net Net-(U5-VI)
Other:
- board text added: "isim yaz"

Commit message: [05] PCB finalized
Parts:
- C8, R12: moved to B.Cu
- R20: moved to F.Cu
- moved R11 187.0 mm to (72.1, 109.4), turned to -90 degrees
- moved R14 137.8 mm to (76.6, 56.1), turned to 180 degrees
- moved C8 97.7 mm to (54.2, 30.4)
- moved R20 55.6 mm to (125.2, 73.7), turned to 180 degrees
- moved R12 31.2 mm to (53.3, 113.2), turned to -90 degrees
- moved R33 14.8 mm to (112.6, 70.6), turned to 180 degrees
- moved J5 5.27 mm to (105.0, 60.0), turned to 0 degrees
- moved U2 4.60 mm to (121.8, 70.5)
- moved R34 1.78 mm to (112.5, 72.9), turned to 0 degrees
- moved J3 1.76 mm to (133.0, 42.5)
- moved J4 1.65 mm to (133.2, 57.7)
- moved C21 1.53 mm to (79.5, 94.5), turned to 0 degrees
- moved R5 1.38 mm to (74.0, 123.0), turned to 180 degrees
- moved R2 1.10 mm to (69.0, 123.5)
- moved F1 1.02 mm to (44.5, 114.0)
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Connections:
- T1 pad 8: (no net) -> GND
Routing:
- net Net-(Q3-E): track 12.2 -> 116.1 mm
- net /Vbias: track 28.4 -> 125.0 mm, vias 1 -> 2
- net /5V: track 0.00 -> 50.0 mm, vias 0 -> 2
- net GND: track 88.8 -> 108.8 mm, vias 3 -> 5
- net /SOUT: track 2.79 -> 16.3 mm
- net Net-(U4-FB): track 8.61 -> 19.1 mm
- net GNDSEC: track 96.2 -> 90.7 mm, vias 1 -> 4
- net Net-(R26-Pad1): track 10.00 -> 15.0 mm
- net PGND: track 25.7 -> 29.0 mm, vias 2 -> 0
- net /GATEOUT: track 50.3 -> 53.4 mm
- net /Isense: track 47.0 -> 49.9 mm
- net Net-(D8-K): track 42.2 -> 39.5 mm
- net Net-(U1-SS_MAXDC): track 7.74 -> 10.4 mm
- net Net-(U4-OPTO): track 2.46 -> 0.00 mm
- net /8V: track 38.0 -> 40.2 mm
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- added copper zone on B.Cu, net /12V
- added copper zone on B.Cu, net /VSEC+
- added copper zone on F.Cu, net /VSEC-
- added copper zone on F.Cu, net /Vaux
- added copper zone on B.Cu, net /Vsw
- added copper zone on B.Cu, net Net-(J3-Pin_1)
- added copper zone on F.Cu, net Net-(R20-Pad2)
- added copper zone on F.Cu, net Net-(U4-OPTO)
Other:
- outline, holes or cut-outs redrawn
- board text added: "ISMACIT - GULSUNA HACETTEPE ELE713 FORWARD CONVERTER 2025"
- board text removed: "isim yaz"
